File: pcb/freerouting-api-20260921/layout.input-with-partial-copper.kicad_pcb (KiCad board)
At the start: 4 copper layers, 36 x 76 mm, 115 parts, among them J1 B2B-PH-K-S, J3 B2B-PH-K-S, J4 104031-0811, Q1 AO3400A, Q2 AO3400A, SW1 PTS841GKSMTR LFS, SW2 JS202011AQN, U1 113991114, U10 SN74CBTLV3245APWR, U11 SN74CBTLV3245APWR, U3 MAX17048G+T10, U4 BMI270, U5 TPS61023DRLR, U6 AP2112K-3.3TRG1, U7 TPS22918DBVR, U8 TPS22918DBVR, U9 TPS22918DBVR

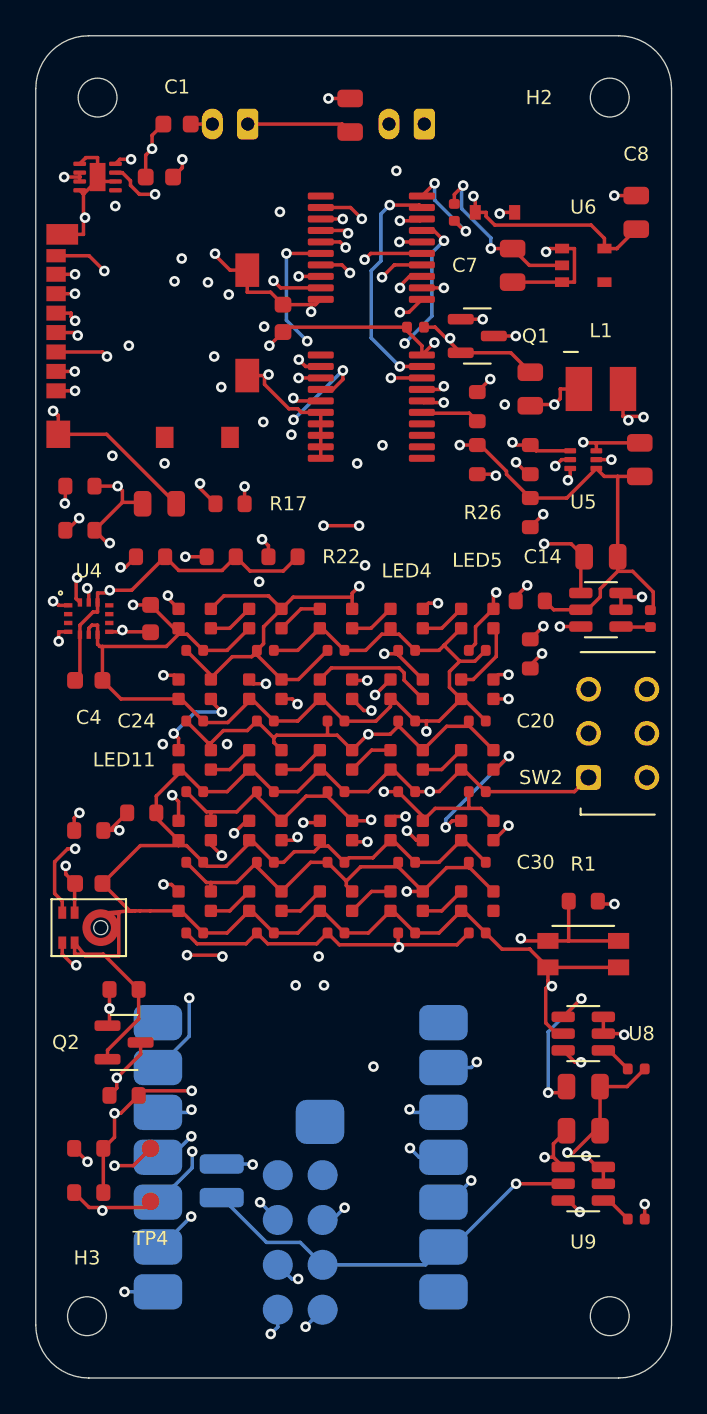
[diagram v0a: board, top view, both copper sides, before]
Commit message: Update board configuration, BOM, and documentation for new XIAO ESP32S3
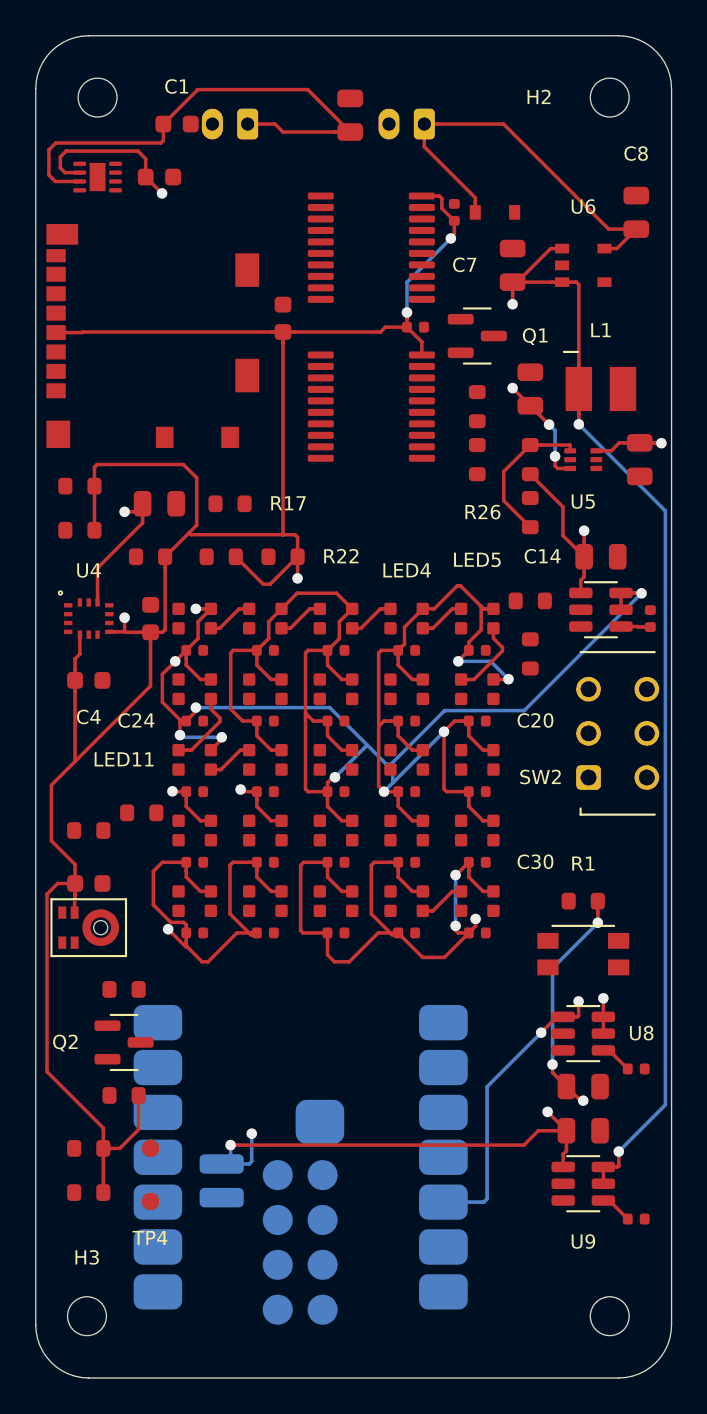
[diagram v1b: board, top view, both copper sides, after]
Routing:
- net GND: track 412.7 -> 0.00 mm, vias 21 -> 0
- net FG_SDA: track 92.1 -> 0.00 mm, vias 7 -> 0
- net FG_SCL: track 86.8 -> 0.00 mm, vias 5 -> 0
- net LED_5V: track 175.9 -> 257.6 mm, vias 12 -> 17
- net VBAT: track 110.1 -> 184.5 mm
- net ISOLATE_N: track 73.0 -> 0.00 mm, vias 4 -> 0
- net HOST_PDM_DATA: track 67.8 -> 0.00 mm, vias 4 -> 0
- net HOST_PDM_CLK: track 63.5 -> 0.00 mm, vias 7 -> 0
- net RUN_ENABLE: track 62.0 -> 0.00 mm, vias 3 -> 0
- net HOST_IMU_INT: track 60.2 -> 0.00 mm, vias 2 -> 0
- net HOST_SD_CS: track 59.8 -> 0.00 mm, vias 2 -> 0
- net HOST_HAPTIC: track 59.5 -> 0.00 mm, vias 4 -> 0
- net HOST_SD_MOSI: track 58.1 -> 0.00 mm, vias 2 -> 0
- net HOST_SD_CLK: track 55.0 -> 0.00 mm, vias 2 -> 0
- net HOST_SD_MISO: track 54.8 -> 0.00 mm, vias 2 -> 0
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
